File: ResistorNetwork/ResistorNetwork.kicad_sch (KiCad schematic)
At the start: 12 parts

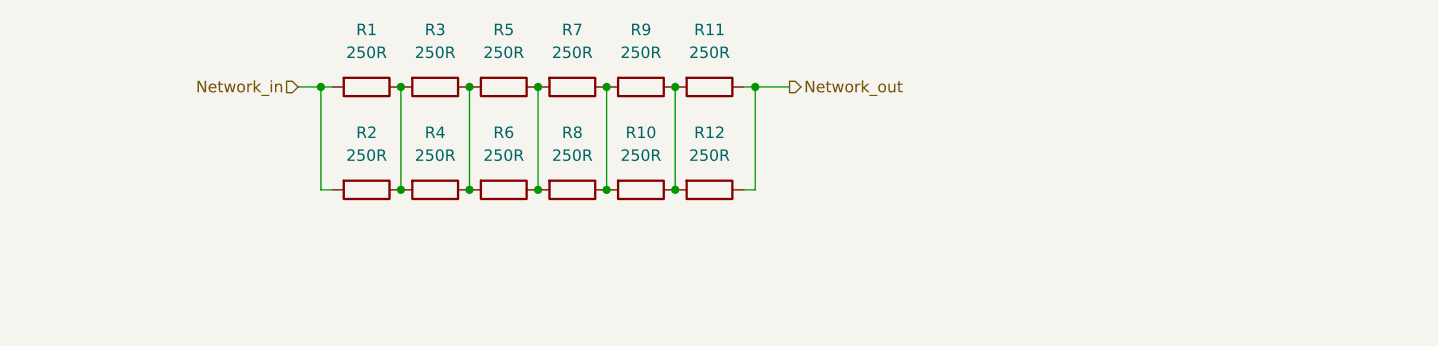
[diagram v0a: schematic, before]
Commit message: resistor network layout done
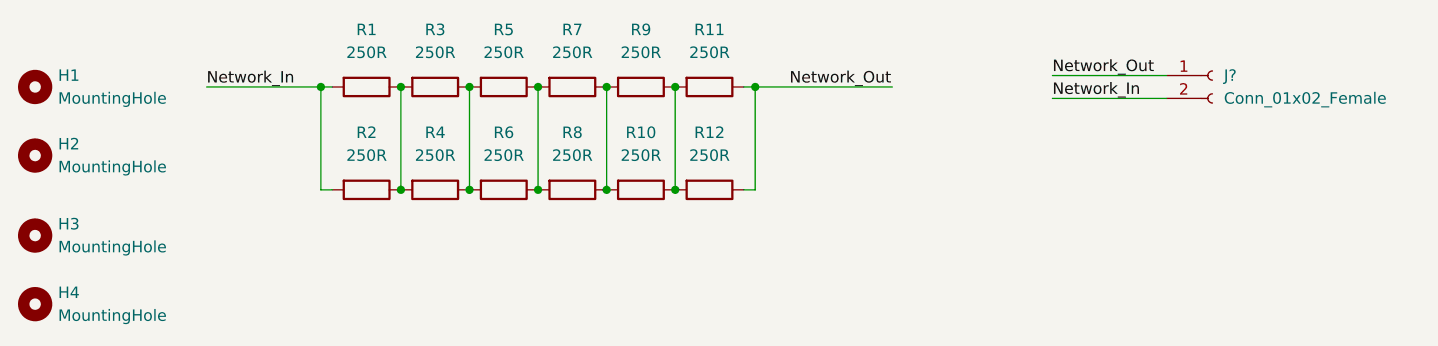
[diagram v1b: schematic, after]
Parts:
- added H1, H2, H3, H4: MountingHole, MountingHole:MountingHole_4.3mm_M4, symbol Mechanical:MountingHole
- added J?: Conn_01x02_Female, symbol Connector:Conn_01x02_Female
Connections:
- net Network_in renamed Network_In
- net Network_In: now also J?.2 (Pin_2)
- net Network_out renamed Network_Out
- net Network_Out: now also J?.1 (Pin_1)
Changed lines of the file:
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@@
+    (stroke (width 0) (type default) (color 0 0 0 0))
+  )
+  (wire (pts (xy 200.66 54.61) (xy 213.36 54.61))
     (stroke (width 0) (type default) (color 0 0 0 0))
   )
@@
     (stroke (width 0) (type default) (color 0 0 0 0))
   )
-  (wire (pts (xy 167.64 55.88) (xy 171.45 55.88))
+  (wire (pts (xy 167.64 55.88) (xy 182.88 55.88))
+    (stroke (width 0) (type default) (color 0 0 0 0))
+  )
+  (wire (pts (xy 200.66 57.15) (xy 213.36 57.15))
     (stroke (width 0) (type default) (color 0 0 0 0))
   )
@@
     (stroke (width 0) (type default) (color 0 0 0 0))
   )
-  (wire (pts (xy 116.84 55.88) (xy 119.38 55.88))
+  (wire (pts (xy 106.68 55.88) (xy 119.38 55.88))
     (stroke (width 0) (type default) (color 0 0 0 0))
   )
@@
     (stroke (width 0) (type default) (color 0 0 0 0))
   )
-  (hierarchical_label "Network_in" (shape input) (at 116.84 55.88 180)
-    (effects (font (size 1.27 1.27)) (justify right))
-  )
-  (hierarchical_label "Network_out" (shape output) (at 171.45 55.88 0)
-    (effects (font (size 1.27 1.27)) (justify left))
+  (label "Network_In" (at 200.66 57.15 0)
+    (effects (font (size 1.27 1.27)) (justify left bottom))
+  )
+  (label "Network_Out" (at 171.45 55.88 0)
+    (effects (font (size 1.27 1.27)) (justify left bottom))
+  )
+  (label "Network_Out" (at 200.66 54.61 0)
+    (effects (font (size 1.27 1.27)) (justify left bottom))
+  )
+  (label "Network_In" (at 106.68 55.88 0)
+    (effects (font (size 1.27 1.27)) (justify left bottom))
   )
   (symbol (lib_id "Device:R") (at 154.94 67.31 270) (unit 1)
@@
     (pin "2")
   )
+  (symbol (lib_id "Mechanical:MountingHole") (at 87.63 80.01 0) (unit 1)
+    (in_bom yes) (on_board yes) (fields_autoplaced)
+    (property "Reference" "H4" (id 0) (at 90.17 78.7399 0)
+      (effects (font (size 1.27 1.27)) (justify left))
+    )
+    (property "Value" "MountingHole" (id 1) (at 90.17 81.2799 0)
+      (effects (font (size 1.27 1.27)) (justify left))
+    )
+    (property "Footprint" "MountingHole:MountingHole_4.3mm_M4" (id 2) (at 87.63 80.01 0)
+      (effects (font (size 1.27 1.27)) hide)
+    )
+    (property "Datasheet" "~" (id 3) (at 87.63 80.01 0)
+      (effects (font (size 1.27 1.27)) hide)
+    )
+  )
   (symbol (lib_id "Device:R") (at 124.46 55.88 270) (unit 1)
     (in_bom yes) (on_board yes) (fields_autoplaced)
@@
     (pin "2")
   )
+  (symbol (lib_id "Mechanical:MountingHole") (at 87.63 55.88 0) (unit 1)
+    (in_bom yes) (on_board yes) (fields_autoplaced)
+    (property "Reference" "H1" (id 0) (at 90.17 54.6099 0)
+      (effects (font (size 1.27 1.27)) (justify left))
+    )
+    (property "Value" "MountingHole" (id 1) (at 90.17 57.1499 0)
+      (effects (font (size 1.27 1.27)) (justify left))
+    )
+    (property "Footprint" "MountingHole:MountingHole_4.3mm_M4" (id 2) (at 87.63 55.88 0)
+      (effects (font (size 1.27 1.27)) hide)
+    )
+    (property "Datasheet" "~" (id 3) (at 87.63 55.88 0)
+      (effects (font (size 1.27 1.27)) hide)
+    )
+  )
   (symbol (lib_id "Device:R") (at 162.56 55.88 270) (unit 1)
     (in_bom yes) (on_board yes) (fields_autoplaced)
@@
     (pin "2")
   )
+  (symbol (lib_id "Mechanical:MountingHole") (at 87.63 72.39 0) (unit 1)
+    (in_bom yes) (on_board yes) (fields_autoplaced)
+    (property "Reference" "H3" (id 0) (at 90.17 71.1199 0)
+      (effects (font (size 1.27 1.27)) (justify left))
+    )
+    (property "Value" "MountingHole" (id 1) (at 90.17 73.6599 0)
+      (effects (font (size 1.27 1.27)) (justify left))
+    )
+    (property "Footprint" "MountingHole:MountingHole_4.3mm_M4" (id 2) (at 87.63 72.39 0)
+      (effects (font (size 1.27 1.27)) hide)
+    )
+    (property "Datasheet" "~" (id 3) (at 87.63 72.39 0)
+      (effects (font (size 1.27 1.27)) hide)
+    )
+  )
   (symbol (lib_id "Device:R") (at 162.56 67.31 270) (unit 1)
     (in_bom yes) (on_board yes) (fields_autoplaced)
@@
     (pin "2")
   )
+  (symbol (lib_id "Connector:Conn_01x02_Female") (at 218.44 54.61 0) (unit 1)
+    (in_bom yes) (on_board yes) (fields_autoplaced)
+    (property "Reference" "J?" (id 0) (at 219.71 54.6099 0)
+      (effects (font (size 1.27 1.27)) (justify left))
+    )
+    (property "Value" "Conn_01x02_Female" (id 1) (at 219.71 57.1499 0)
+      (effects (font (size 1.27 1.27)) (justify left))
+    )
+    (property "Footprint" "" (id 2) (at 218.44 54.61 0)
+      (effects (font (size 1.27 1.27)) hide)
+    )
+    (property "Datasheet" "~" (id 3) (at 218.44 54.61 0)
+      (effects (font (size 1.27 1.27)) hide)
+    )
+    (pin "1")
+    (pin "2")
+  )
+  (symbol (lib_id "Mechanical:MountingHole") (at 87.63 63.5 0) (unit 1)
+    (in_bom yes) (on_board yes) (fields_autoplaced)
+    (property "Reference" "H2" (id 0) (at 90.17 62.2299 0)
+      (effects (font (size 1.27 1.27)) (justify left))
+    )
+    (property "Value" "MountingHole" (id 1) (at 90.17 64.7699 0)
+      (effects (font (size 1.27 1.27)) (justify left))
+    )
+    (property "Footprint" "MountingHole:MountingHole_4.3mm_M4" (id 2) (at 87.63 63.5 0)
+      (effects (font (size 1.27 1.27)) hide)
+    )
+    (property "Datasheet" "~" (id 3) (at 87.63 63.5 0)
+      (effects (font (size 1.27 1.27)) hide)
+    )
+  )
   (symbol (lib_id "Device:R") (at 147.32 67.31 270) (unit 1)
     (in_bom yes) (on_board yes) (fields_autoplaced)
@@
   )
   (symbol_instances
+    (path "/5b78bd78-66b9-42dc-90f6-6ff1e98a07c3"
+      (reference "H1") (unit 1) (value "MountingHole") (footprint "MountingHole:MountingHole_4.3mm_M4")
+    )
+    (path "/f5ea3923-be33-43be-9e5e-f1bf8301255e"
+      (reference "H2") (unit 1) (value "MountingHole") (footprint "MountingHole:MountingHole_4.3mm_M4")
+    )
+    (path "/c64fdb2b-35aa-479c-b963-978113bf1fcf"
+      (reference "H3") (unit 1) (value "MountingHole") (footprint "MountingHole:MountingHole_4.3mm_M4")
+    )
+    (path "/3053891a-5d0f-43e6-ad2a-3863ecb75e84"
+      (reference "H4") (unit 1) (value "MountingHole") (footprint "MountingHole:MountingHole_4.3mm_M4")
+    )
+    (path "/ed028af3-7480-48c5-9fd0-a0c44d06b57e"
+      (reference "J?") (unit 1) (value "Conn_01x02_Female") (footprint "")
+    )
     (path "/4b22eaf9-e238-481a-a665-90415c6d0c4a"
       (reference "R1") (unit 1) (value "250R") (footprint "Package_TO_SOT_SMD:TO-263-2_TabPin1")

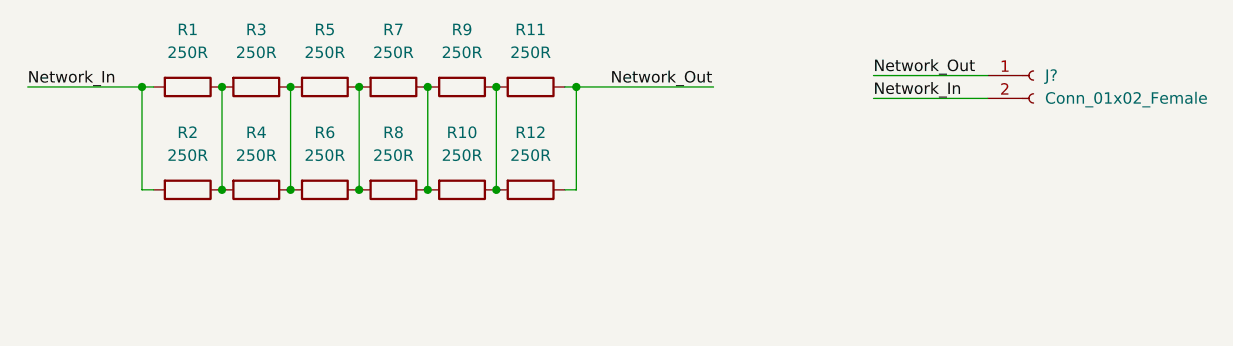
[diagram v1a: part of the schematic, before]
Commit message: adjusted resistor values to match thermal requirements
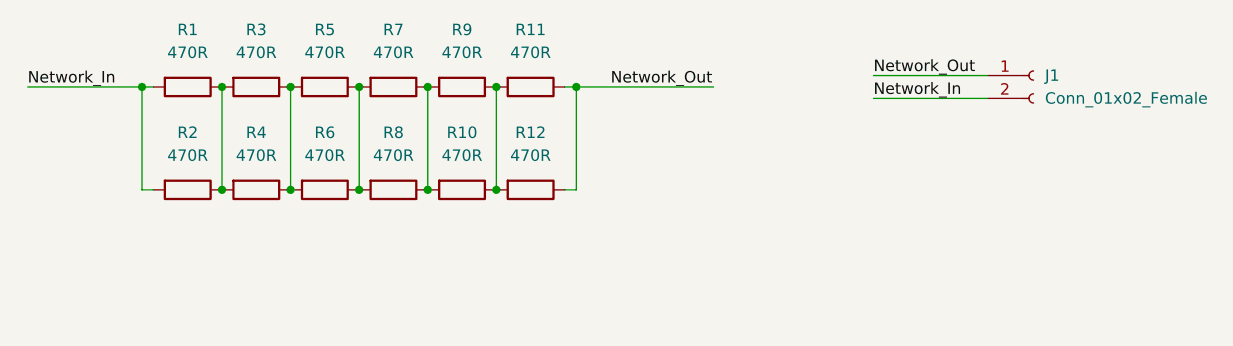
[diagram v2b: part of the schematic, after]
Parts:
- J1: renamed from J?; footprint (none) -> Connector_Molex:Molex_Micro-Fit_3.0_43045-0210_2x01-1MP_P3.00mm_Horizontal
- R1, R10, R11, R12, R2, R3, R4, R5, R6, R7, R8, R9: value 250R -> 470R
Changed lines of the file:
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@@
     (in_bom yes) (on_board yes) (fields_autoplaced)
     (property "Reference" "R10" (id 0) (at 154.94 60.96 90))
-    (property "Value" "250R" (id 1) (at 154.94 63.5 90))
+    (property "Value" "470R" (id 1) (at 154.94 63.5 90))
     (property "Footprint" "Package_TO_SOT_SMD:TO-263-2_TabPin1" (id 2) (at 154.94 65.532 90)
       (effects (font (size 1.27 1.27)) hide)
@@
     (in_bom yes) (on_board yes) (fields_autoplaced)
     (property "Reference" "R1" (id 0) (at 124.46 49.53 90))
-    (property "Value" "250R" (id 1) (at 124.46 52.07 90))
+    (property "Value" "470R" (id 1) (at 124.46 52.07 90))
     (property "Footprint" "Package_TO_SOT_SMD:TO-263-2_TabPin1" (id 2) (at 124.46 54.102 90)
       (effects (font (size 1.27 1.27)) hide)
@@
     (in_bom yes) (on_board yes) (fields_autoplaced)
     (property "Reference" "R7" (id 0) (at 147.32 49.53 90))
-    (property "Value" "250R" (id 1) (at 147.32 52.07 90))
+    (property "Value" "470R" (id 1) (at 147.32 52.07 90))
     (property "Footprint" "Package_TO_SOT_SMD:TO-263-2_TabPin1" (id 2) (at 147.32 54.102 90)
       (effects (font (size 1.27 1.27)) hide)
@@
     (in_bom yes) (on_board yes) (fields_autoplaced)
     (property "Reference" "R11" (id 0) (at 162.56 49.53 90))
-    (property "Value" "250R" (id 1) (at 162.56 52.07 90))
+    (property "Value" "470R" (id 1) (at 162.56 52.07 90))
     (property "Footprint" "Package_TO_SOT_SMD:TO-263-2_TabPin1" (id 2) (at 162.56 54.102 90)
       (effects (font (size 1.27 1.27)) hide)
@@
     (in_bom yes) (on_board yes) (fields_autoplaced)
     (property "Reference" "R3" (id 0) (at 132.08 49.53 90))
-    (property "Value" "250R" (id 1) (at 132.08 52.07 90))
+    (property "Value" "470R" (id 1) (at 132.08 52.07 90))
     (property "Footprint" "Package_TO_SOT_SMD:TO-263-2_TabPin1" (id 2) (at 132.08 54.102 90)
       (effects (font (size 1.27 1.27)) hide)
@@
     (in_bom yes) (on_board yes) (fields_autoplaced)
     (property "Reference" "R5" (id 0) (at 139.7 49.53 90))
-    (property "Value" "250R" (id 1) (at 139.7 52.07 90))
+    (property "Value" "470R" (id 1) (at 139.7 52.07 90))
     (property "Footprint" "Package_TO_SOT_SMD:TO-263-2_TabPin1" (id 2) (at 139.7 54.102 90)
       (effects (font (size 1.27 1.27)) hide)
@@
     (in_bom yes) (on_board yes) (fields_autoplaced)
     (property "Reference" "R4" (id 0) (at 132.08 60.96 90))
-    (property "Value" "250R" (id 1) (at 132.08 63.5 90))
+    (property "Value" "470R" (id 1) (at 132.08 63.5 90))
     (property "Footprint" "Package_TO_SOT_SMD:TO-263-2_TabPin1" (id 2) (at 132.08 65.532 90)
       (effects (font (size 1.27 1.27)) hide)
@@
     (in_bom yes) (on_board yes) (fields_autoplaced)
     (property "Reference" "R9" (id 0) (at 154.94 49.53 90))
-    (property "Value" "250R" (id 1) (at 154.94 52.07 90))
+    (property "Value" "470R" (id 1) (at 154.94 52.07 90))
     (property "Footprint" "Package_TO_SOT_SMD:TO-263-2_TabPin1" (id 2) (at 154.94 54.102 90)
       (effects (font (size 1.27 1.27)) hide)
@@
     (in_bom yes) (on_board yes) (fields_autoplaced)
     (property "Reference" "R12" (id 0) (at 162.56 60.96 90))
-    (property "Value" "250R" (id 1) (at 162.56 63.5 90))
+    (property "Value" "470R" (id 1) (at 162.56 63.5 90))
     (property "Footprint" "Package_TO_SOT_SMD:TO-263-2_TabPin1" (id 2) (at 162.56 65.532 90)
       (effects (font (size 1.27 1.27)) hide)
@@
     (in_bom yes) (on_board yes) (fields_autoplaced)
     (property "Reference" "R2" (id 0) (at 124.46 60.96 90))
-    (property "Value" "250R" (id 1) (at 124.46 63.5 90))
+    (property "Value" "470R" (id 1) (at 124.46 63.5 90))
     (property "Footprint" "Package_TO_SOT_SMD:TO-263-2_TabPin1" (id 2) (at 124.46 65.532 90)
       (effects (font (size 1.27 1.27)) hide)
@@
     (in_bom yes) (on_board yes) (fields_autoplaced)
     (property "Reference" "R6" (id 0) (at 139.7 60.96 90))
-    (property "Value" "250R" (id 1) (at 139.7 63.5 90))
+    (property "Value" "470R" (id 1) (at 139.7 63.5 90))
     (property "Footprint" "Package_TO_SOT_SMD:TO-263-2_TabPin1" (id 2) (at 139.7 65.532 90)
       (effects (font (size 1.27 1.27)) hide)
@@
   (symbol (lib_id "Connector:Conn_01x02_Female") (at 218.44 54.61 0) (unit 1)
     (in_bom yes) (on_board yes) (fields_autoplaced)
-    (property "Reference" "J?" (id 0) (at 219.71 54.6099 0)
+    (property "Reference" "J1" (id 0) (at 219.71 54.6099 0)
       (effects (font (size 1.27 1.27)) (justify left))
     )
@@
       (effects (font (size 1.27 1.27)) (justify left))
     )
-    (property "Footprint" "" (id 2) (at 218.44 54.61 0)
+    (property "Footprint" "Connector_Molex:Molex_Micro-Fit_3.0_43045-0210_2x01-1MP_P3.00mm_Horizontal" (id 2) (at 218.44 54.61 0)
       (effects (font (size 1.27 1.27)) hide)
     )
@@
     (in_bom yes) (on_board yes) (fields_autoplaced)
     (property "Reference" "R8" (id 0) (at 147.32 60.96 90))
-    (property "Value" "250R" (id 1) (at 147.32 63.5 90))
+    (property "Value" "470R" (id 1) (at 147.32 63.5 90))
     (property "Footprint" "Package_TO_SOT_SMD:TO-263-2_TabPin1" (id 2) (at 147.32 65.532 90)
       (effects (font (size 1.27 1.27)) hide)
@@
     )
     (path "/ed028af3-7480-48c5-9fd0-a0c44d06b57e"
-      (reference "J?") (unit 1) (value "Conn_01x02_Female") (footprint "")
+      (reference "J1") (unit 1) (value "Conn_01x02_Female") (footprint "Connector_Molex:Molex_Micro-Fit_3.0_43045-0210_2x01-1MP_P3.00mm_Horizontal")
     )
     (path "/4b22eaf9-e238-481a-a665-90415c6d0c4a"
-      (reference "R1") (unit 1) (value "250R") (footprint "Package_TO_SOT_SMD:TO-263-2_TabPin1")
+      (reference "R1") (unit 1) (value "470R") (footprint "Package_TO_SOT_SMD:TO-263-2_TabPin1")
     )
     (path "/d35d4476-f427-4031-92b2-6182675c88f7"
-      (reference "R2") (unit 1) (value "250R") (footprint "Package_TO_SOT_SMD:TO-263-2_TabPin1")
+      (reference "R2") (unit 1) (value "470R") (footprint "Package_TO_SOT_SMD:TO-263-2_TabPin1")
     )
     (path "/7b1ab658-d87f-41fa-9a03-d6e8f8c61bd5"
-      (reference "R3") (unit 1) (value "250R") (footprint "Package_TO_SOT_SMD:TO-263-2_TabPin1")
+      (reference "R3") (unit 1) (value "470R") (footprint "Package_TO_SOT_SMD:TO-263-2_TabPin1")
     )
     (path "/9786d51d-7516-4d37-ac71-6dbff564d338"
-      (reference "R4") (unit 1) (value "250R") (footprint "Package_TO_SOT_SMD:TO-263-2_TabPin1")
+      (reference "R4") (unit 1) (value "470R") (footprint "Package_TO_SOT_SMD:TO-263-2_TabPin1")
     )
     (path "/8beda06c-9206-4a8b-b0a7-cdcf6f2c4dd5"
-      (reference "R5") (unit 1) (value "250R") (footprint "Package_TO_SOT_SMD:TO-263-2_TabPin1")
+      (reference "R5") (unit 1) (value "470R") (footprint "Package_TO_SOT_SMD:TO-263-2_TabPin1")
     )
     (path "/d8fafb01-aae5-445b-8056-99d168e48b56"
-      (reference "R6") (unit 1) (value "250R") (footprint "Package_TO_SOT_SMD:TO-263-2_TabPin1")
+      (reference "R6") (unit 1) (value "470R") (footprint "Package_TO_SOT_SMD:TO-263-2_TabPin1")
     )
     (path "/57e79ca5-e895-4bbb-9e93-7bf9ba9277c7"
-      (reference "R7") (unit 1) (value "250R") (footprint "Package_TO_SOT_SMD:TO-263-2_TabPin1")
+      (reference "R7") (unit 1) (value "470R") (footprint "Package_TO_SOT_SMD:TO-263-2_TabPin1")
     )
     (path "/ff99d28b-7316-4da5-b859-2e4426080452"
-      (reference "R8") (unit 1) (value "250R") (footprint "Package_TO_SOT_SMD:TO-263-2_TabPin1")
+      (reference "R8") (unit 1) (value "470R") (footprint "Package_TO_SOT_SMD:TO-263-2_TabPin1")
     )
     (path "/c2e7b7c2-b7a4-46d5-86b8-73bb97745a2b"
-      (reference "R9") (unit 1) (value "250R") (footprint "Package_TO_SOT_SMD:TO-263-2_TabPin1")
+      (reference "R9") (unit 1) (value "470R") (footprint "Package_TO_SOT_SMD:TO-263-2_TabPin1")
     )
     (path "/0945556f-2a92-4f8e-8185-cb020e1e0b49"
-      (reference "R10") (unit 1) (value "250R") (footprint "Package_TO_SOT_SMD:TO-263-2_TabPin1")
+      (reference "R10") (unit 1) (value "470R") (footprint "Package_TO_SOT_SMD:TO-263-2_TabPin1")
     )
     (path "/71a847a8-e6a3-469e-b190-a8e1c063cdda"
-      (reference "R11") (unit 1) (value "250R") (footprint "Package_TO_SOT_SMD:TO-263-2_TabPin1")
+      (reference "R11") (unit 1) (value "470R") (footprint "Package_TO_SOT_SMD:TO-263-2_TabPin1")
     )
     (path "/c9b51d0a-8cbc-44d2-a339-3c2b0d2ee049"
-      (reference "R12") (unit 1) (value "250R") (footprint "Package_TO_SOT_SMD:TO-263-2_TabPin1")
-    )
-  )
+      (reference "R12") (unit 1) (value "470R") (footprint "Package_TO_SOT_SMD:TO-263-2_TabPin1")
+    )
+  )
